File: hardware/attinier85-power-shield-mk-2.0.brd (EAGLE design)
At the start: 36 x 25 mm, 6 parts, among them IC1 MC34063DIP, U1 ATTINIEST85_SHIELDV2

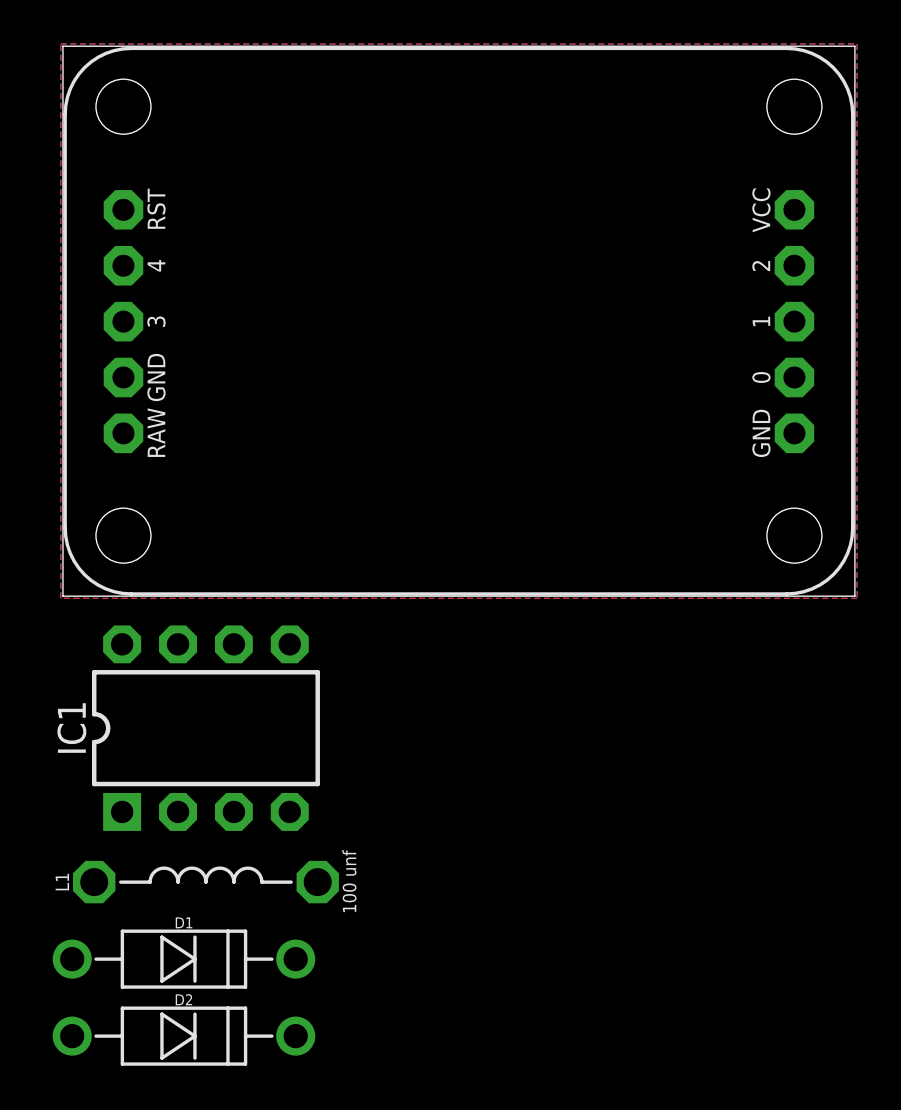
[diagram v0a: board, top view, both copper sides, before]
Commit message: renaming parts
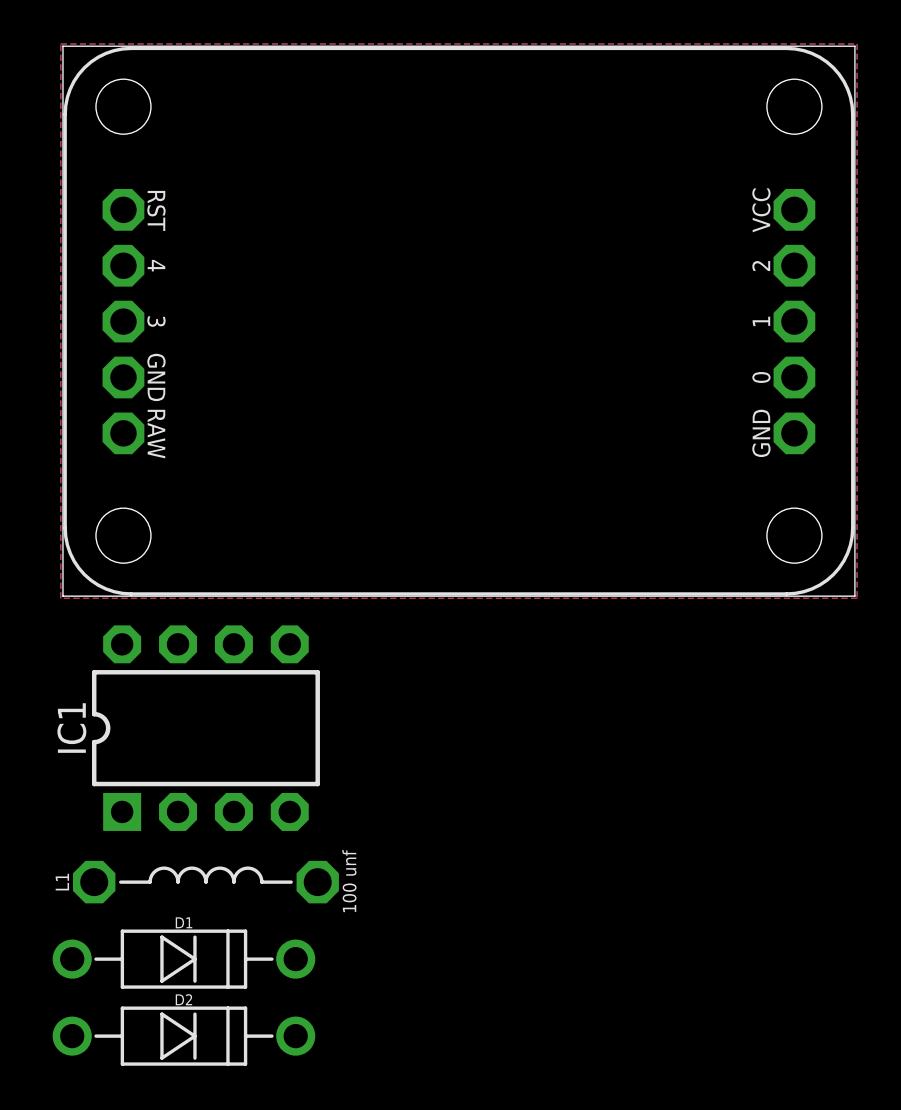
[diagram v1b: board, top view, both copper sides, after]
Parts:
- U1: value ATTINIEST85_SHIELDV2 -> ATTINIER85_SHIELDV2; device A_butts:ATTINIEST85_SHIELD_V2 -> A_butts:ATTINIER85_SHIELD_V2
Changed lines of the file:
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@@
 <attribute name="DESIGNER" value="Nobody" x="13.97" y="-1.27" size="1.778" layer="27" display="off"/>
 </element>
-<element name="U1" library="A_butts" package="ATTINIEST85_SHIELD_V2" value="ATTINIEST85_SHIELDV2" x="18" y="12.5"/>
+<element name="U1" library="A_butts" package="ATTINIER85_SHIELD_V2" value="ATTINIER85_SHIELDV2" x="18" y="12.5"/>
 <element name="IC1" library="A_butts" package="DIP-08" value="MC34063DIP" x="6.5" y="-6"/>
 <element name="L1" library="A_butts" package="INDUCTOR-AXIAL-PTH-10.16MM" value="100 unf" x="6.5" y="-13"/>
